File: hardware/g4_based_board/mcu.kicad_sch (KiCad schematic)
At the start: 23 parts, among them Q3 PMOS, Q4 PMOS, SW1 SW_SPDT, SW2 RESET, U1 STM32G431CBTx, Y1 12MHz, 20pF

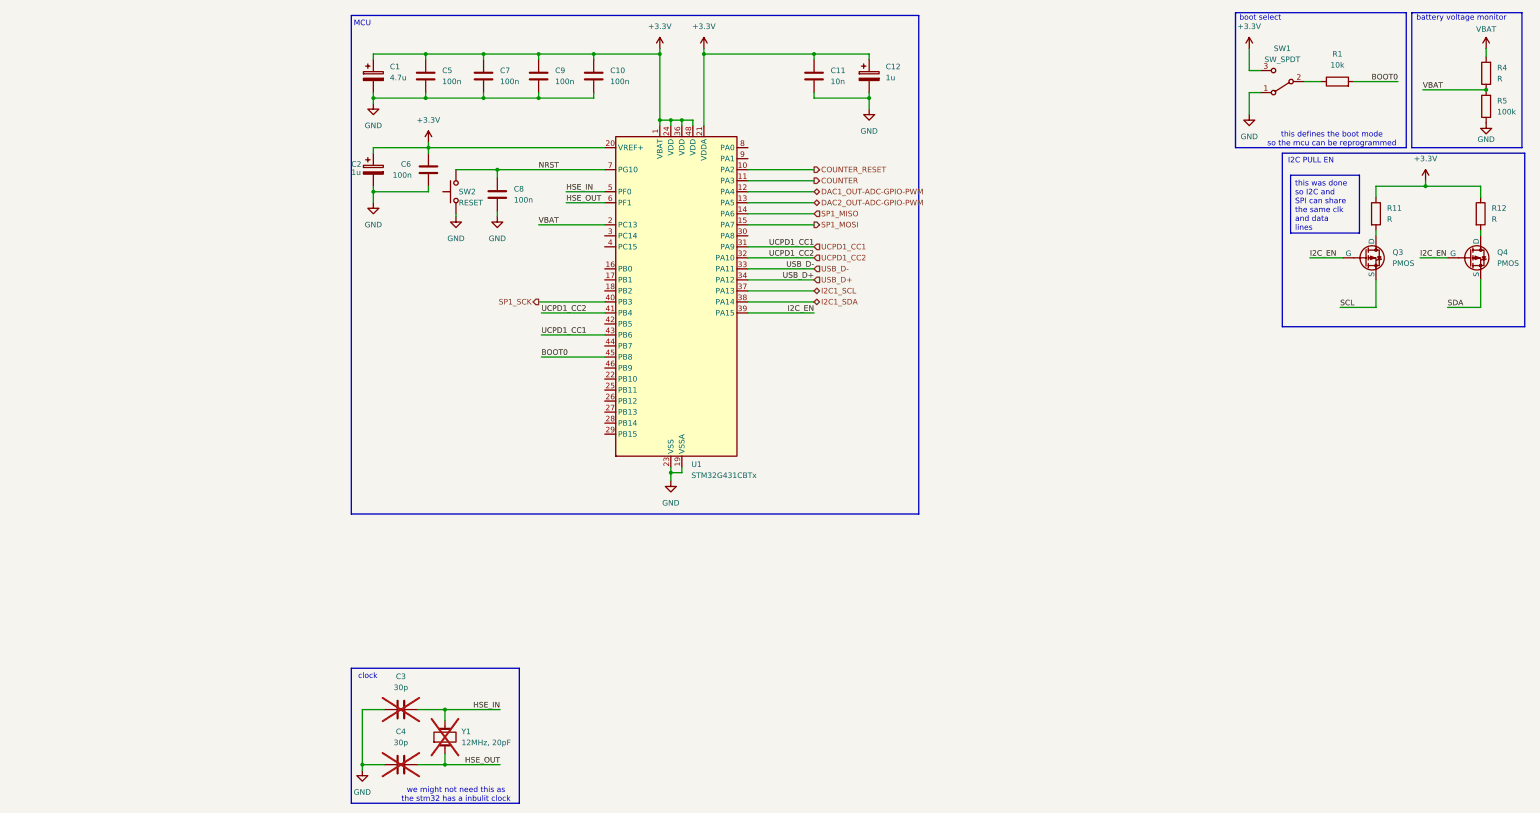
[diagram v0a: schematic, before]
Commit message: added more hierarchical ports and removed the i2c pull ups
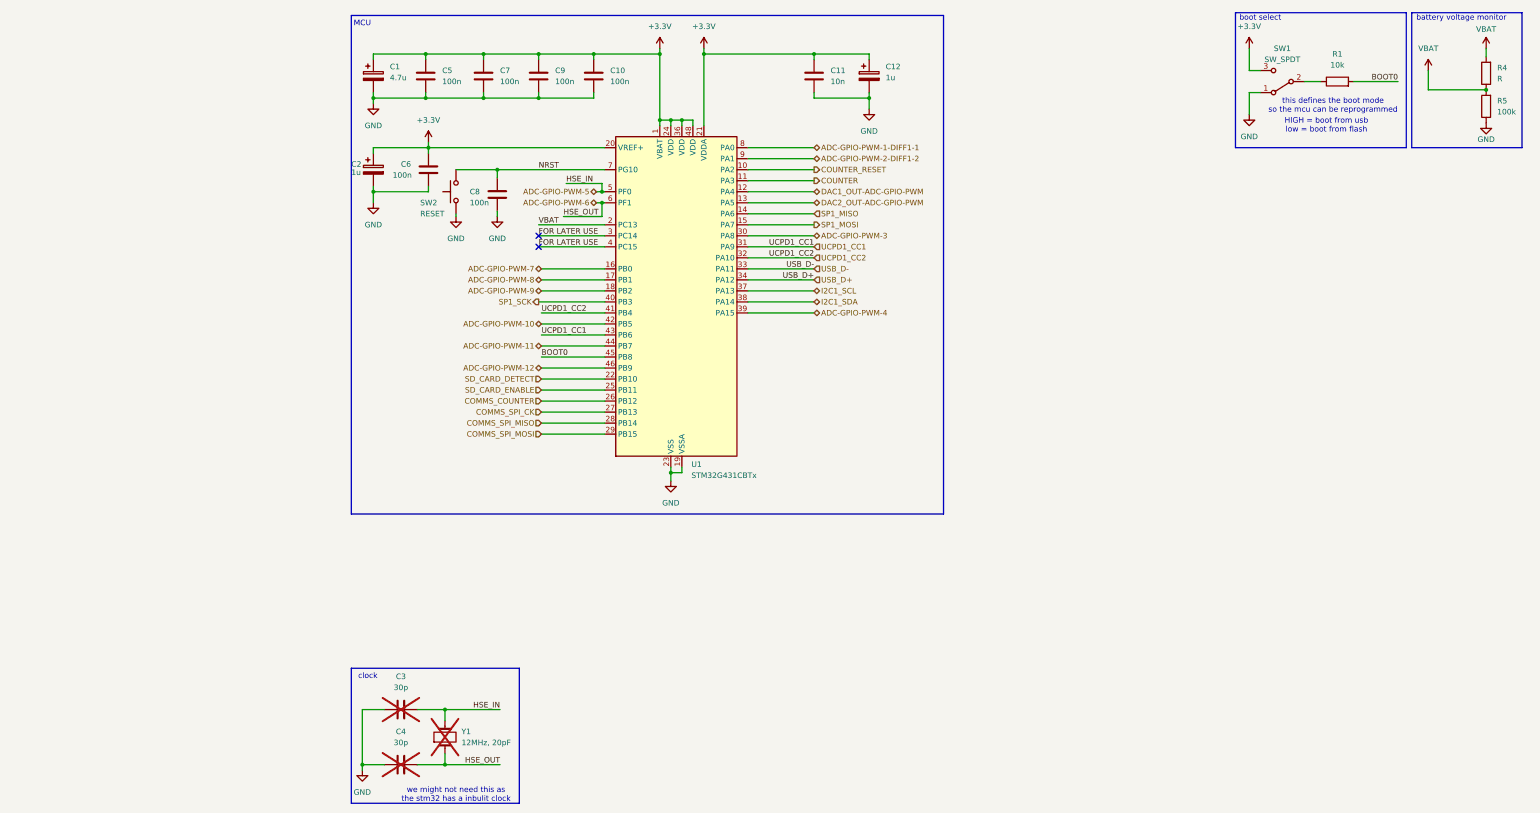
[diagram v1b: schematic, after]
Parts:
- removed Q3, Q4: PMOS, Package_TO_SOT_SMD:TSOT-23, symbol Simulation_SPICE:PMOS
- removed R11, R12: R, Resistor_SMD:R_0805_2012Metric, symbol Device:R
- R1, R4, R5: footprint Resistor_SMD:R_0805_2012Metric_Pad1.20x1.40mm_HandSolder -> Resistor_SMD:R_0805_2012Metric
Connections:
- net ADC-GPIO-PWM-7: now reaches U1.16 (PB0)
- net ADC-GPIO-PWM-8: now reaches U1.17 (PB1)
- net ADC-GPIO-PWM-9: now reaches U1.18 (PB2)
- net SD_CARD_DETECT: now reaches U1.22 (PB10)
- net SD_CARD_ENABLE: now reaches U1.25 (PB11)
- net COMMS_COUNTER: now reaches U1.26 (PB12)
- net COMMS_SPI_CK: now reaches U1.27 (PB13)
- net COMMS_SPI_MISO: now reaches U1.28 (PB14)
- net COMMS_SPI_MOSI: now reaches U1.29 (PB15)
- net FOR LATER USE: now reaches U1.3 (PC14)
- net FOR LATER USE: now also U1.4 (PC15)
- net ADC-GPIO-PWM-3: now reaches U1.30 (PA8)
- net ADC-GPIO-PWM-10: now reaches U1.42 (PB5)
- net ADC-GPIO-PWM-11: now reaches U1.44 (PB7)
- net ADC-GPIO-PWM-12: now reaches U1.46 (PB9)
- net ADC-GPIO-PWM-1-DIFF1-1: now reaches U1.8 (PA0)
- net ADC-GPIO-PWM-2-DIFF1-2: now reaches U1.9 (PA1)
- net HSE_IN renamed ADC-GPIO-PWM-5
- net HSE_OUT renamed ADC-GPIO-PWM-6
- net I2C_EN renamed ADC-GPIO-PWM-4
- no-connect marks 0 -> 2
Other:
- note added: "HIGH = boot from usb"
- note added: "low = boot from flash"
- note removed: "I2C PULL EN"

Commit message: removed comms counter and it now uses the one defined in spi_en_expander
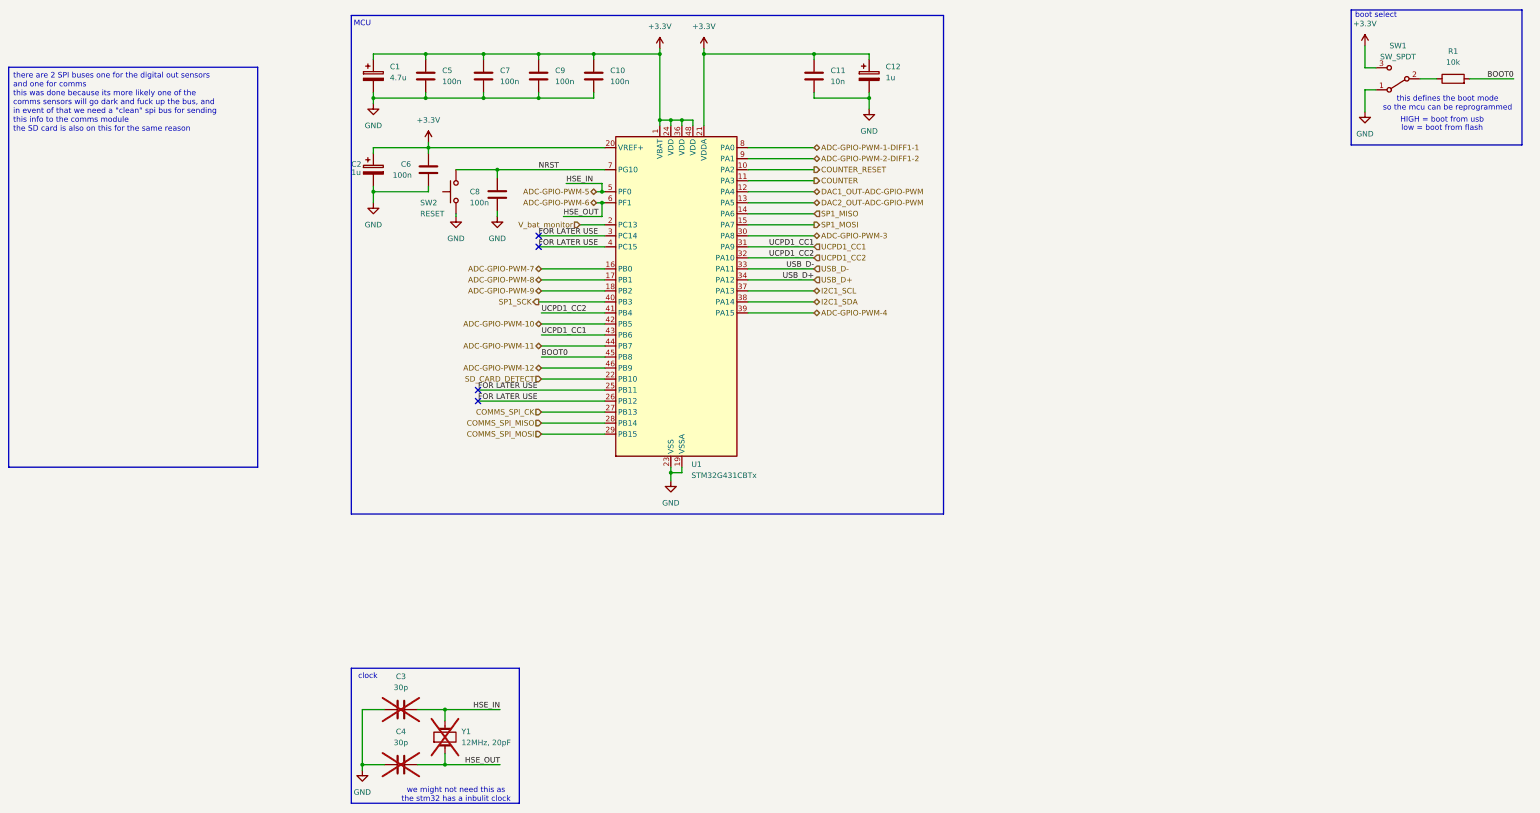
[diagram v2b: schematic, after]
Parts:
- removed R4: R, Resistor_SMD:R_0805_2012Metric, symbol Device:R
- removed R5: 100k, Resistor_SMD:R_0805_2012Metric, symbol Device:R
- C1, C10, C11, C12, C2, C3, C4, C5, C6, C7, C8, C9: footprint Capacitor_SMD:C_0805_2012Metric -> Capacitor_SMD:C_0603_1608Metric_Pad1.08x0.95mm_HandSolder
- R1: footprint Resistor_SMD:R_0805_2012Metric -> Resistor_SMD:R_0603_1608Metric_Pad0.98x0.95mm_HandSolder
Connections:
- net COMMS_COUNTER is gone; now on net FOR LATER USE: U1.26 (PB12)
- net SD_CARD_ENABLE is gone; now on net FOR LATER USE: U1.25 (PB11)
- net VBAT renamed V_bat_monitor
- no-connect marks 2 -> 4
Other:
- note removed: "battery voltage monitor"
- moved on the sheet: R1, SW1

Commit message: change mcu to a larger version of the stm32G4 allowing for the spi expander to be removed
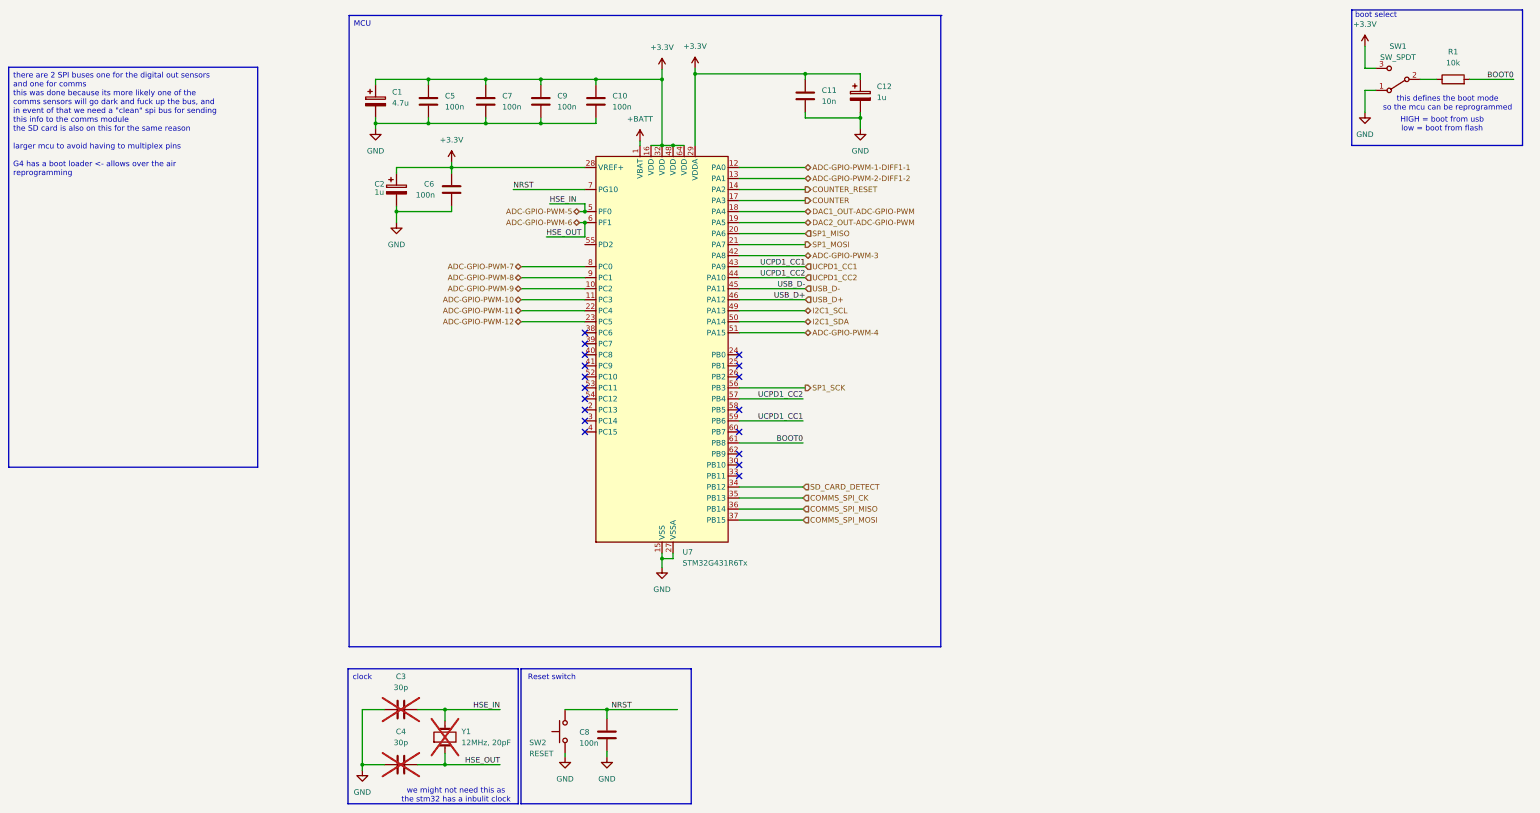
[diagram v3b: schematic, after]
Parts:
- removed U1: STM32G431CBTx, Package_QFP:LQFP-48_7x7mm_P0.5mm, symbol MCU_ST_STM32G4:STM32G431CBTx
- added U7: STM32G431R6Tx, Package_QFP:LQFP-64_10x10mm_P0.5mm, symbol MCU_ST_STM32G4:STM32G431R6Tx
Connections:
- net +3.3V: now also U7.16 (VDD), U7.28 (VREF+), U7.29 (VDDA), U7.32 (VDD), U7.48 (VDD), U7.64 (VDD)
- net ADC-GPIO-PWM-1-DIFF1-1: now also U7.12 (PA0)
- net ADC-GPIO-PWM-10: now also U7.11 (PC3)
- net ADC-GPIO-PWM-11: now also U7.22 (PC4)
- net ADC-GPIO-PWM-12: now also U7.23 (PC5)
- net ADC-GPIO-PWM-2-DIFF1-2: now also U7.13 (PA1)
- net ADC-GPIO-PWM-3: now also U7.42 (PA8)
- net ADC-GPIO-PWM-4: now also U7.51 (PA15)
- net ADC-GPIO-PWM-5: now also U7.5 (PF0)
- net ADC-GPIO-PWM-6: now also U7.6 (PF1)
- net ADC-GPIO-PWM-7: now also U7.8 (PC0)
- net ADC-GPIO-PWM-8: now also U7.9 (PC1)
- net ADC-GPIO-PWM-9: now also U7.10 (PC2)
- net BOOT0: now also U7.61 (PB8)
- net COMMS_SPI_CK: now also U7.35 (PB13)
- net COMMS_SPI_MISO: now also U7.36 (PB14)
- net COMMS_SPI_MOSI: now also U7.37 (PB15)
- net COUNTER: now also U7.17 (PA3)
- net COUNTER_RESET: now also U7.14 (PA2)
- net DAC1_OUT-ADC-GPIO-PWM: now also U7.18 (PA4)
- net DAC2_OUT-ADC-GPIO-PWM: now also U7.19 (PA5)
- net GND: now also U7.15 (VSS), U7.27 (VSSA), U7.31 (VSS), U7.47 (VSS), U7.63 (VSS)
- net I2C1_SCL: now also U7.49 (PA13)
- net I2C1_SDA: now also U7.50 (PA14)
- net NRST: now also U7.7 (PG10)
- net SD_CARD_DETECT: now also U7.34 (PB12)
- net SP1_MISO: now also U7.20 (PA6)
- net SP1_MOSI: now also U7.21 (PA7)
- net SP1_SCK: now also U7.56 (PB3)
- net UCPD1_CC1: now also U7.43 (PA9), U7.59 (PB6)
- net UCPD1_CC2: now also U7.44 (PA10), U7.57 (PB4)
- net USB_D+: now also U7.46 (PA12)
- net USB_D-: now also U7.45 (PA11)
- new net +BATT: U7.1 (VBAT)
- no-connect marks 4 -> 18
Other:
- note added: "Reset switch"

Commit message: removed spi expander and now uses mcu pins for enable
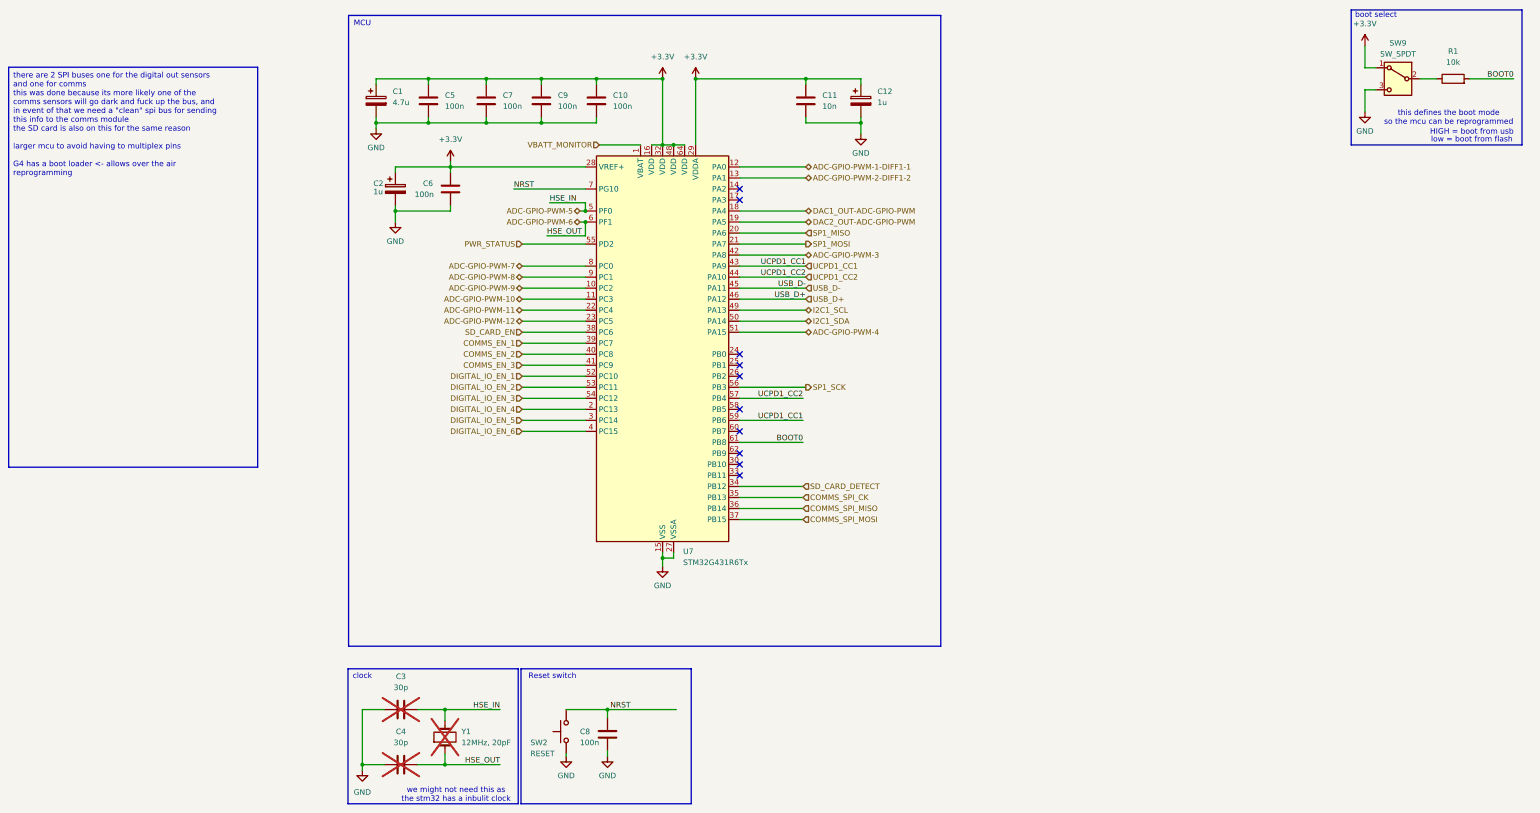
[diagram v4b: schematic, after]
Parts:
- removed SW1: SW_SPDT, Button_Switch_THT:SW_Slide_SPDT_Angled_CK_OS102011MA1Q, symbol Switch:SW_SPDT
- added SW9: SW_SPDT, Button_Switch_THT:SW_Slide_SPDT_Angled_CK_OS102011MA1Q, symbol Switch:SW_SPDT
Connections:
- net +3.3V: now also SW9.1 (A)
- net GND: now also SW9.3 (C)
- net at R1.1: now also SW9.2 (B)
- net DIGITAL_IO_EN_4: now reaches U7.2 (PC13)
- net DIGITAL_IO_EN_5: now reaches U7.3 (PC14)
- net SD_CARD_EN: now reaches U7.38 (PC6)
- net COMMS_EN_1: now reaches U7.39 (PC7)
- net DIGITAL_IO_EN_6: now reaches U7.4 (PC15)
- net COMMS_EN_2: now reaches U7.40 (PC8)
- net COMMS_EN_3: now reaches U7.41 (PC9)
- net DIGITAL_IO_EN_1: now reaches U7.52 (PC10)
- net DIGITAL_IO_EN_2: now reaches U7.53 (PC11)
- net DIGITAL_IO_EN_3: now reaches U7.54 (PC12)
- net PWR_STATUS: now reaches U7.55 (PD2)
- net +BATT renamed VBATT_MONITOR
- net COUNTER: no longer names the net of U7.17 (PA3)
- net COUNTER_RESET: no longer names the net of U7.14 (PA2)
- no-connect marks 18 -> 10
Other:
- moved on the sheet: C11, C12
